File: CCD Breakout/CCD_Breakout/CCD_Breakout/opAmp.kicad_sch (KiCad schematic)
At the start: 1 part, among them U8 OPA4322AIPWR

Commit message: CCD Footprints
ADC and CCD footprints needed
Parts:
- U8: footprint PW14_TEX -> (none)
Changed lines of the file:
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@@
 			)
 		)
-		(property "Footprint" "PW14_TEX"
+		(property "Footprint" ""
 			(at 102.87 88.9 0)
 			(effects

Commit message: Fixed CCD Footprints
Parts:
- U8: footprint (none) -> CCD:OPA4322AIPWR
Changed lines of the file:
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@@
 			)
 		)
-		(property "Footprint" ""
+		(property "Footprint" "CCD:OPA4322AIPWR"
 			(at 102.87 88.9 0)
 			(effects

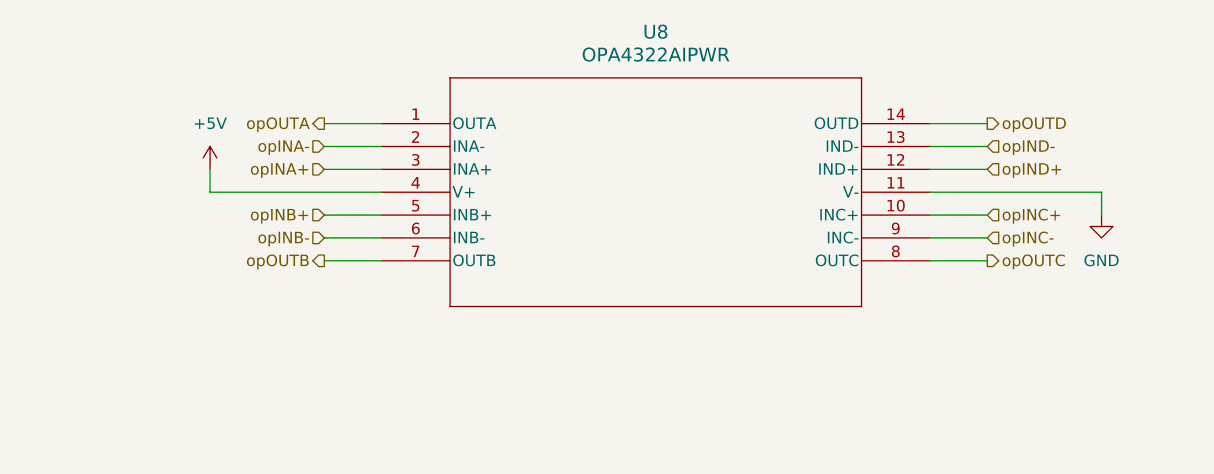
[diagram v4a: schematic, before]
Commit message: OP amp filtered
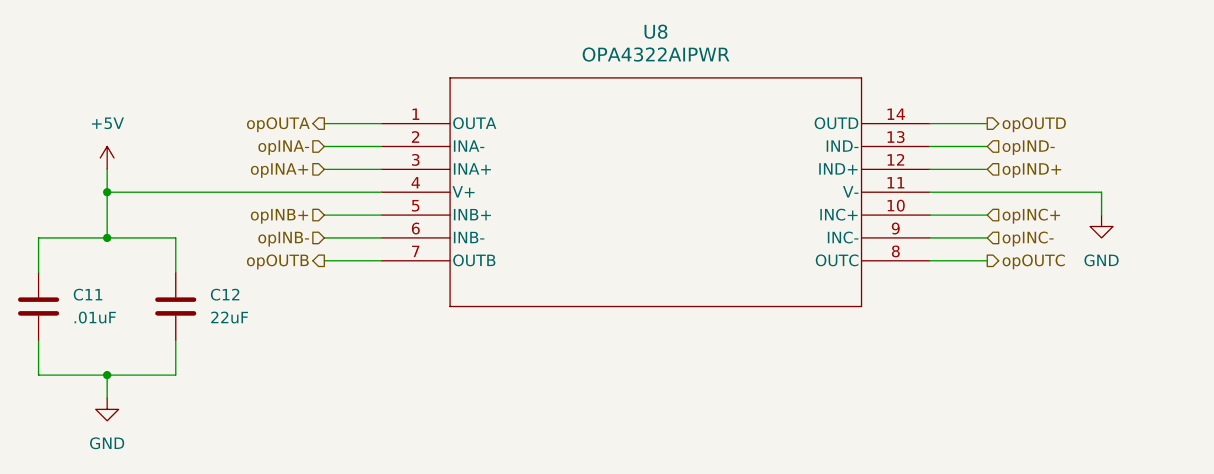
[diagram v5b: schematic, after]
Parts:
- added C11: .01uF, Capacitor_SMD:C_0603_1608Metric_Pad1.08x0.95mm_HandSolder, symbol Device:C
- added C12: 22uF, Capacitor_SMD:C_0603_1608Metric_Pad1.08x0.95mm_HandSolder, symbol Device:C
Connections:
- net +5V: now also C11.1, C12.1
- net GND: now also C11.2, C12.2

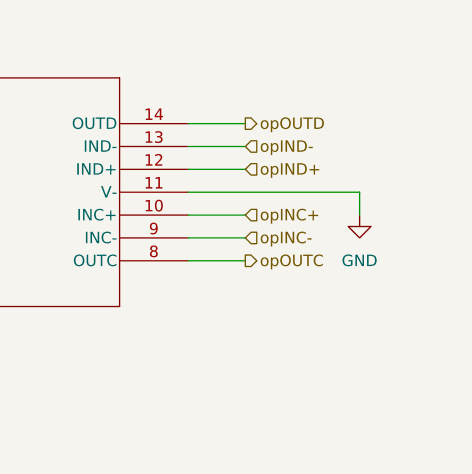
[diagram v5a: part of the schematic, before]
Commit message: Board redesign for laser engraving
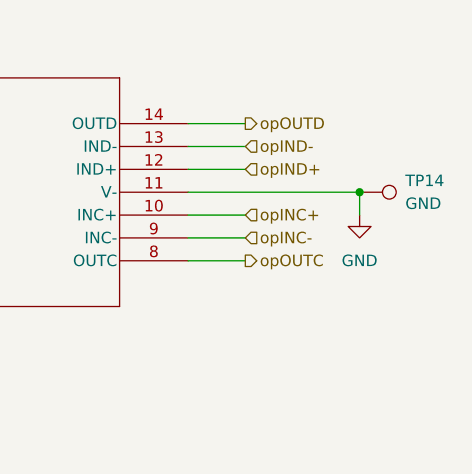
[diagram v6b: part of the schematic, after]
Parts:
- added TP14: GND, TestPoint:TestPoint_Pad_D1.0mm, symbol Connector:TestPoint
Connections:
- net GND: now also TP14.1
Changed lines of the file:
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@@
+		(color 0 0 0 0)
+	)
+	(junction
+		(at 182.88 96.52)
+		(diameter 0)
 		(color 0 0 0 0)
 	)
@@
 					(unit 1)
 				)
+			)
+		)
+	)
+	(symbol
+		(lib_id "Connector:TestPoint")
+		(at 182.88 96.52 270)
+		(unit 1)
+		(exclude_from_sim no)
+		(in_bom yes)
+		(on_board yes)
+		(dnp no)
+		(fields_autoplaced yes)
+		(property "Reference" "TP14"
+			(at 187.96 95.2499 90)
+			(effects
+				(font
+					(size 1.27 1.27)
+				)
+				(justify left)
+			)
+		)
+		(property "Value" "GND"
+			(at 187.96 97.7899 90)
+			(effects
+				(font
+					(size 1.27 1.27)
+				)
+				(justify left)
+			)
+		)
+		(property "Footprint" "TestPoint:TestPoint_Pad_D1.0mm"
+			(at 182.88 101.6 0)
+			(effects
+				(font
+					(size 1.27 1.27)
+				)
+				(hide yes)
+			)
+		)
+		(property "Datasheet" "~"
+			(at 182.88 101.6 0)
+			(effects
+				(font
+					(size 1.27 1.27)
+				)
+				(hide yes)
+			)
+		)
+		(property "Description" "test point"
+			(at 182.88 96.52 0)
+			(effects
+				(font
+					(size 1.27 1.27)
+				)
+				(hide yes)
+			)
+		)
+		(pin "1"
+		)
+		(instances
+			(project "CCD_Breakout"
+				(path "/102965ac-29c6-4f96-94a4-d07431f6d693/1e63b7fc-fcaa-417b-98e4-15f8c0595846"
+					(reference "TP14")
+					(unit 1)
+				)
